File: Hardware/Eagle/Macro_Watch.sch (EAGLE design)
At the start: 40 parts, among them M1 MF-LED-0603-RED, M16 MF-LED-0603-RED, M2 MF-LED-0603-RED, M32 MF-LED-0603-RED, M4 MF-LED-0603-RED, M8 MF-LED-0603-RED, U1 EFM8SB10F2G-A-QFN20R, X1 ECS-.327-12.5-34B-TR

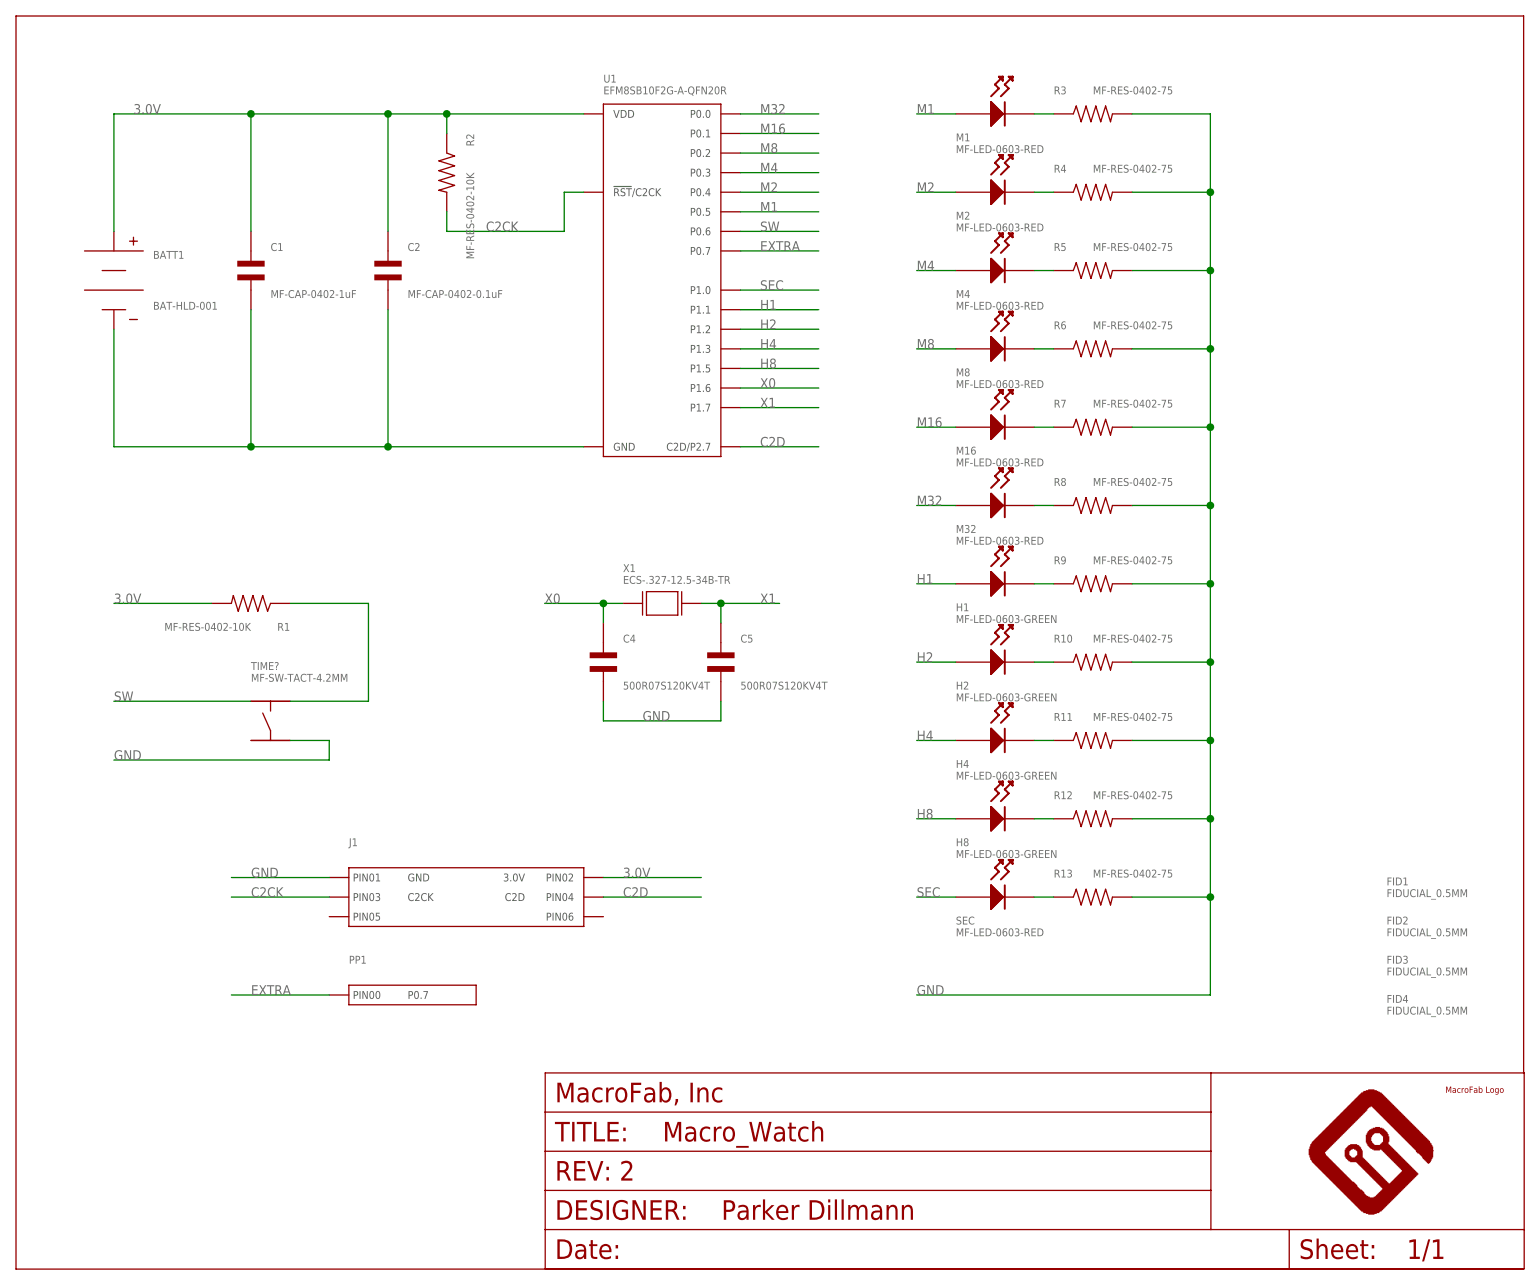
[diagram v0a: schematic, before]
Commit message: Updated files to latest Library.
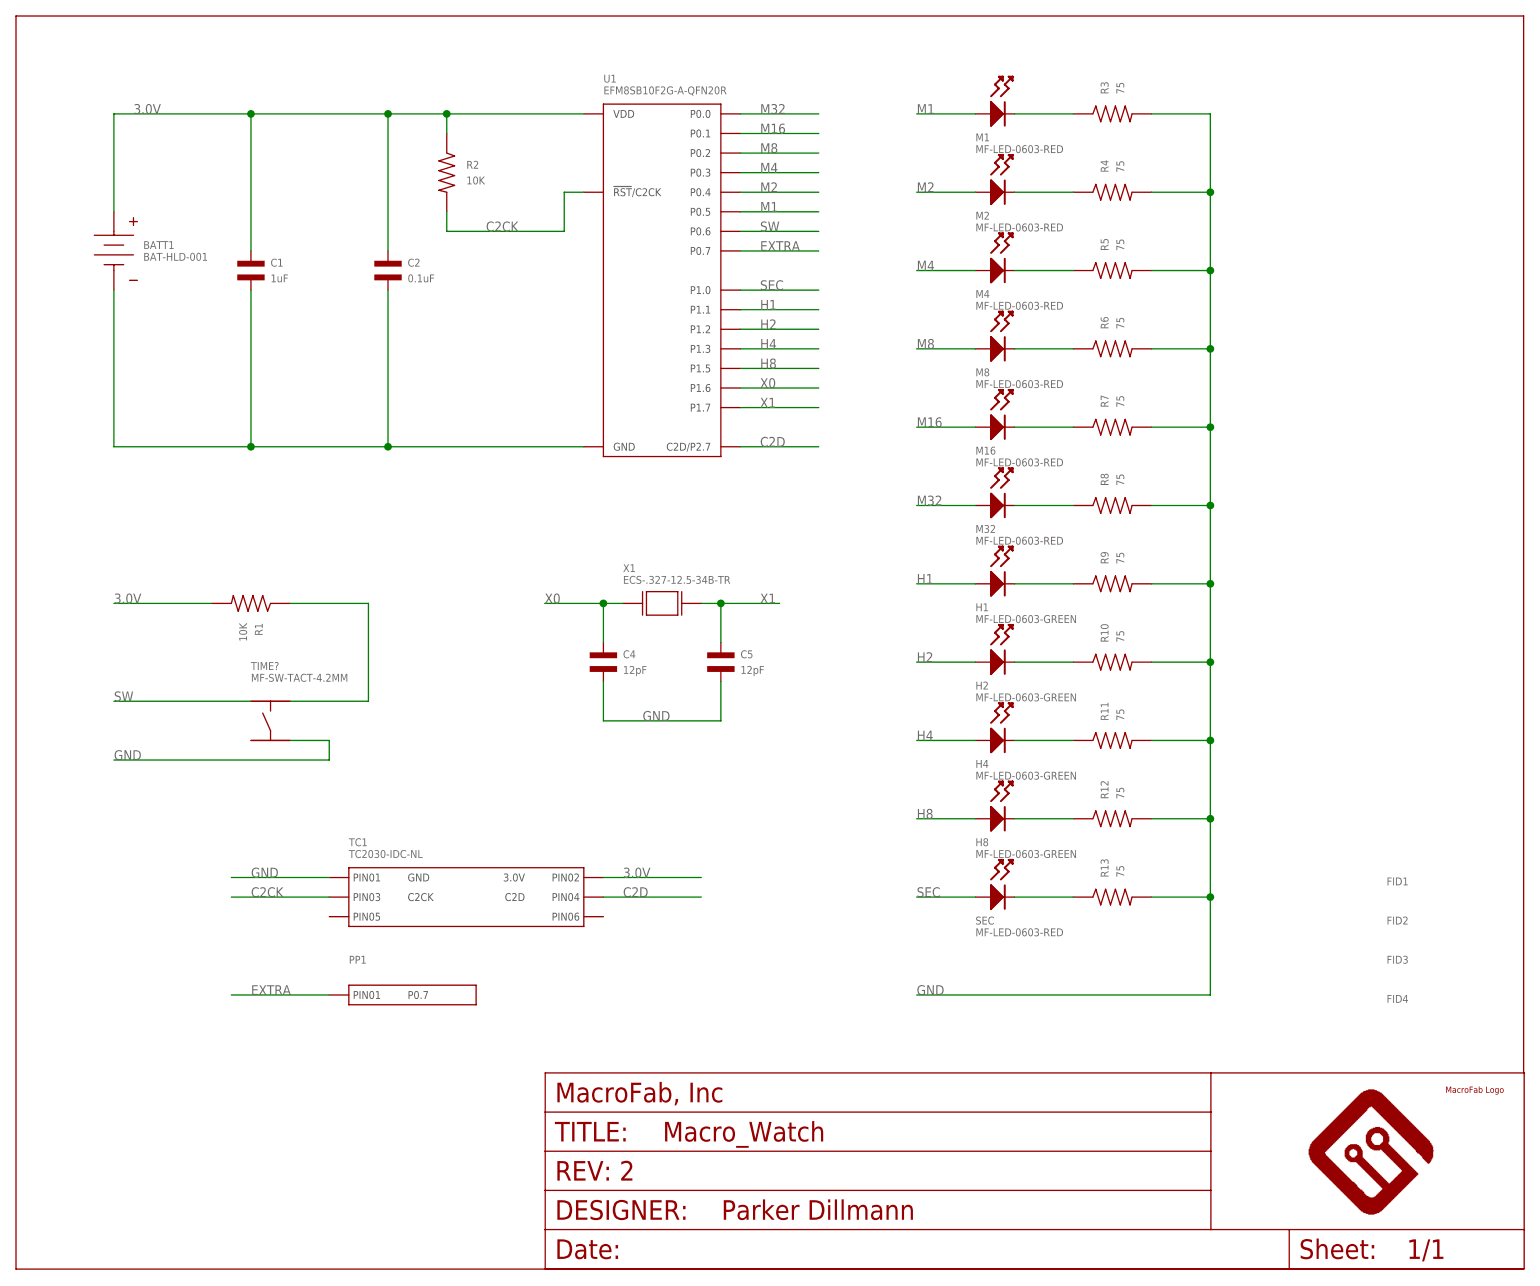
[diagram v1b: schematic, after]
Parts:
- removed J1: (no value), PP_Connectors:CON_02X03_TC2030
- added TC1: TC2030-IDC-NL, MF_Connectors:CON_02X03_TC2030-IDC-NL
- C1: value MF-CAP-0402-1uF -> 1uF; MPN (none) -> MF-CAP-0402-1uF
- C2: value MF-CAP-0402-0.1uF -> 0.1uF; MPN (none) -> MF-CAP-0402-0.1uF
- C4, C5: value 500R07S120KV4T -> 12pF; MPN (none) -> 500R07S120KV4T
- H1, H2, H4, H8: device MF_LEDs:LED_SINGLE_0603 -> MF_LEDs:LED_SINGLE-0603-GREEN
- M1, M16, M2, M32, M4, M8, SEC: device MF_LEDs:LED_SINGLE_0603 -> MF_LEDs:LED_SINGLE-0603-RED
- PP1: device MF_Connectors:POGO_PIN_01X01 -> MF_Connectors:POGO_PIN_01X01_70-9150; LABEL00 P0.7 -> (none); LABEL01 (none) -> P0.7; POPULATE (none) -> 0
- R1, R2: value MF-RES-0402-10K -> 10K; MPN (none) -> MF-RES-0402-10K
- R10, R11, R12, R13, R3, R4, R5, R6, R7, R8, R9: value MF-RES-0402-75 -> 75; MPN (none) -> MF-RES-0402-75
- U1: MPN (none) -> EFM8SB10F2G-A-QFN20R
- X1: device MF_Frequency_Control:ECX-31B -> MF_Frequency_Control:CYRSTAL_ECX-31B; MPN (none) -> ECS-.327-12.5-34B-TR
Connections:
- net 3.0V: now also TC1.PIN2; no longer J1.PIN2
- net C2CK: now also TC1.PIN3; no longer J1.PIN3
- net C2D: now also TC1.PIN4; no longer J1.PIN4
- net EXTRA: now also PP1.PIN1; no longer PP1.PIN0
- net GND: now also TC1.PIN1; no longer J1.PIN1
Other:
- moved on the sheet: R1, R10, R11, R12, R13, R2, R3, R4, R5, R6, R7, R8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
